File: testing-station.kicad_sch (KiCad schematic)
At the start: 0 parts

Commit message: added MAX31865 schematic page
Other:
- added sheet MAX31865 (MAX31865.kicad_sch)
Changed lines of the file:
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@@
 	(generator_version "8.0")
 	(paper "A4")
+	(sheet
+		(at 52.705 43.18)
+		(size 14.605 13.335)
+		(fields_autoplaced yes)
+		(stroke
+			(width 0.1524)
+			(type solid)
+		)
+		(fill
+			(color 0 0 0 0.0000)
+		)
+		(property "Sheetname" "MAX31865"
+			(at 52.705 42.4684 0)
+			(effects
+				(font
+					(size 1.27 1.27)
+				)
+				(justify left bottom)
+			)
+		)
+		(property "Sheetfile" "MAX31865.kicad_sch"
+			(at 52.705 57.0996 0)
+			(effects
+				(font
+					(size 1.27 1.27)
+				)
+				(justify left top)
+			)
+		)
+		(pin "SCK" input
+			(at 67.31 45.72 0)
+			(effects
+				(font
+					(size 1.27 1.27)
+				)
+				(justify right)
+			)
+		)
+		(pin "MISO" input
+			(at 67.31 48.26 0)
+			(effects
+				(font
+					(size 1.27 1.27)
+				)
+				(justify right)
+			)
+		)
+		(pin "CS" input
+			(at 67.31 50.8 0)
+			(effects
+				(font
+					(size 1.27 1.27)
+				)
+				(justify right)
+			)
+		)
+		(pin "MOSI" input
+			(at 67.31 53.34 0)
+			(effects
+				(font
+					(size 1.27 1.27)
+				)
+				(justify right)
+			)
+		)
+		(instances
+			(project "testing-station"
+				(path "/ed3950ec-e24f-4dd6-b9cc-eca012f1333b"
+					(page "2")
+				)
+			)
+		)
+	)
 	(sheet_instances
 		(path "/"

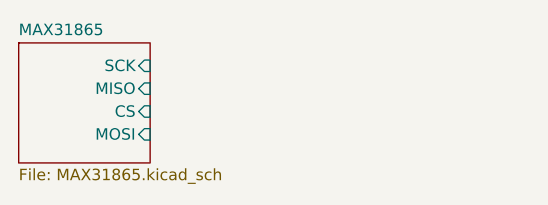
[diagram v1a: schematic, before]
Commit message: added BME680 schematic page
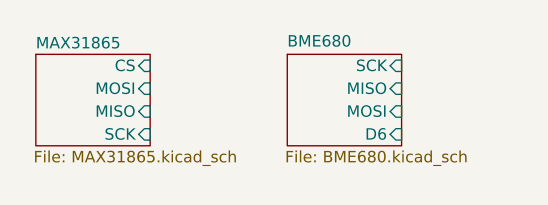
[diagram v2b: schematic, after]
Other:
- added sheet BME680 (BME680.kicad_sch)
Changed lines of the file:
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@@
 	(paper "A4")
 	(sheet
-		(at 52.705 43.18)
-		(size 14.605 13.335)
-		(fields_autoplaced yes)
+		(at 82.55 44.45)
+		(size 12.7 10.16)
+		(stroke
+			(width 0.1524)
+			(type solid)
+		)
+		(fill
+			(color 0 0 0 0.0000)
+		)
+		(property "Sheetname" "BME680"
+			(at 82.55 43.7384 0)
+			(effects
+				(font
+					(size 1.27 1.27)
+				)
+				(justify left bottom)
+			)
+		)
+		(property "Sheetfile" "BME680.kicad_sch"
+			(at 82.296 55.118 0)
+			(effects
+				(font
+					(size 1.27 1.27)
+				)
+				(justify left top)
+			)
+		)
+		(pin "MOSI" input
+			(at 95.25 50.8 0)
+			(effects
+				(font
+					(size 1.27 1.27)
+				)
+				(justify right)
+			)
+		)
+		(pin "D6" input
+			(at 95.25 53.34 0)
+			(effects
+				(font
+					(size 1.27 1.27)
+				)
+				(justify right)
+			)
+		)
+		(pin "MISO" input
+			(at 95.25 48.26 0)
+			(effects
+				(font
+					(size 1.27 1.27)
+				)
+				(justify right)
+			)
+		)
+		(pin "SCK" input
+			(at 95.25 45.72 0)
+			(effects
+				(font
+					(size 1.27 1.27)
+				)
+				(justify right)
+			)
+		)
+		(instances
+			(project "testing-station"
+				(path "/ed3950ec-e24f-4dd6-b9cc-eca012f1333b"
+					(page "3")
+				)
+			)
+		)
+	)
+	(sheet
+		(at 54.61 44.45)
+		(size 12.7 10.16)
 		(stroke
 			(width 0.1524)
@@
 		)
 		(property "Sheetname" "MAX31865"
-			(at 52.705 42.4684 0)
+			(at 54.61 43.942 0)
 			(effects
 				(font
@@
 		)
 		(property "Sheetfile" "MAX31865.kicad_sch"
-			(at 52.705 57.0996 0)
+			(at 54.356 55.118 0)
 			(effects
 				(font
@@
 		)
 		(pin "SCK" input
+			(at 67.31 53.34 0)
+			(effects
+				(font
+					(size 1.27 1.27)
+				)
+				(justify right)
+			)
+		)
+		(pin "MISO" input
+			(at 67.31 50.8 0)
+			(effects
+				(font
+					(size 1.27 1.27)
+				)
+				(justify right)
+			)
+		)
+		(pin "CS" input
 			(at 67.31 45.72 0)
 			(effects
@@
 			)
 		)
-		(pin "MISO" input
+		(pin "MOSI" input
 			(at 67.31 48.26 0)
 			(effects
 				(font
-					(size 1.27 1.27)
-				)
-				(justify right)
-			)
-		)
-		(pin "CS" input
-			(at 67.31 50.8 0)
-			(effects
-				(font
-					(size 1.27 1.27)
-				)
-				(justify right)
-			)
-		)
-		(pin "MOSI" input
-			(at 67.31 53.34 0)
-			(effects
-				(font

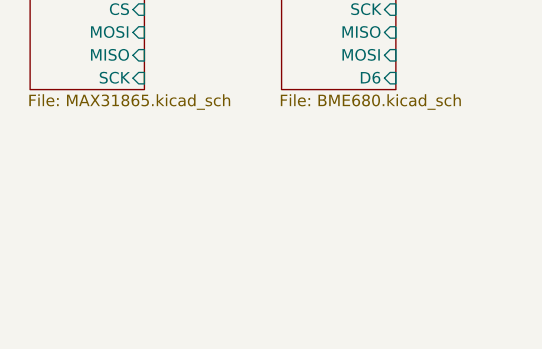
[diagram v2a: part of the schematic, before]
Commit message: added DS3231 schematic page
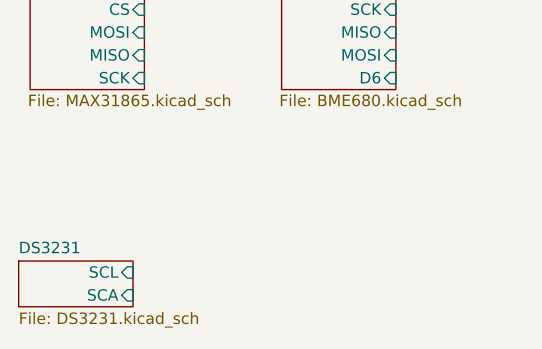
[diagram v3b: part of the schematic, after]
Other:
- added sheet DS3231 (DS3231.kicad_sch)
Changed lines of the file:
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@@
 	(paper "A4")
+	(sheet
+		(at 53.34 73.66)
+		(size 12.7 5.08)
+		(fields_autoplaced yes)
+		(stroke
+			(width 0.1524)
+			(type solid)
+		)
+		(fill
+			(color 0 0 0 0.0000)
+		)
+		(property "Sheetname" "DS3231"
+			(at 53.34 72.9484 0)
+			(effects
+				(font
+					(size 1.27 1.27)
+				)
+				(justify left bottom)
+			)
+		)
+		(property "Sheetfile" "DS3231.kicad_sch"
+			(at 53.34 79.3246 0)
+			(effects
+				(font
+					(size 1.27 1.27)
+				)
+				(justify left top)
+			)
+		)
+		(pin "SCL" input
+			(at 66.04 74.93 0)
+			(effects
+				(font
+					(size 1.27 1.27)
+				)
+				(justify right)
+			)
+		)
+		(pin "SCA" input
+			(at 66.04 77.47 0)
+			(effects
+				(font
+					(size 1.27 1.27)
+				)
+				(justify right)
+			)
+		)
+		(instances
+			(project "testing-station"
+				(path "/ed3950ec-e24f-4dd6-b9cc-eca012f1333b"
+					(page "4")
+				)
+			)
+		)
+	)
 	(sheet
 		(at 82.55 44.45)

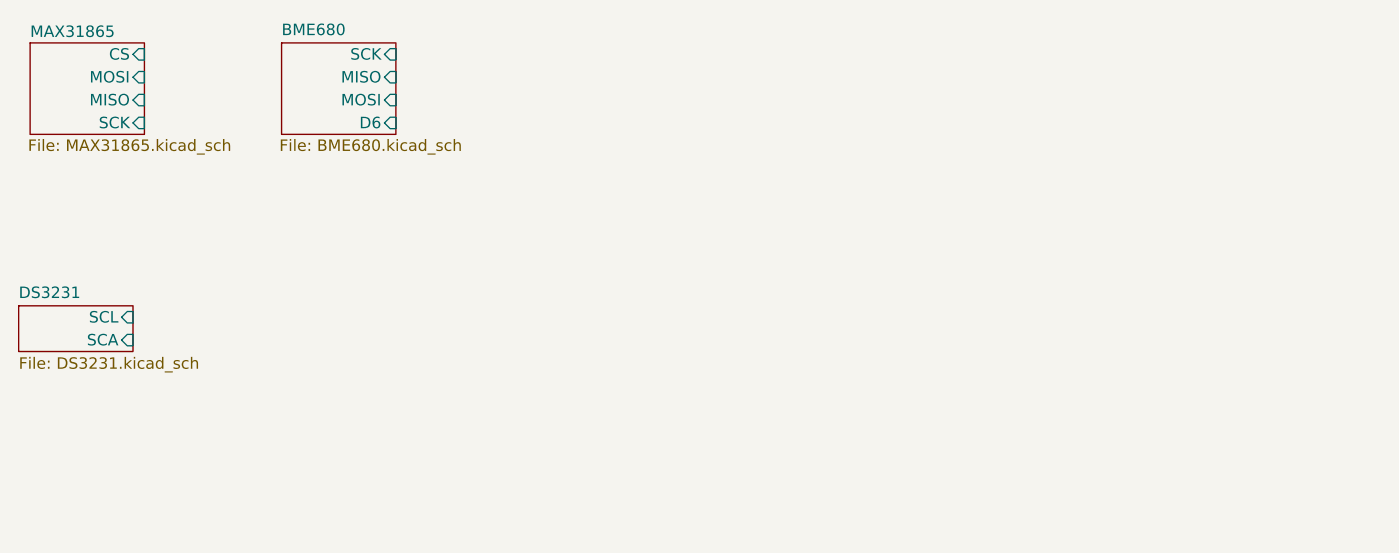
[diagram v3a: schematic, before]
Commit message: added 2 more MAX31865
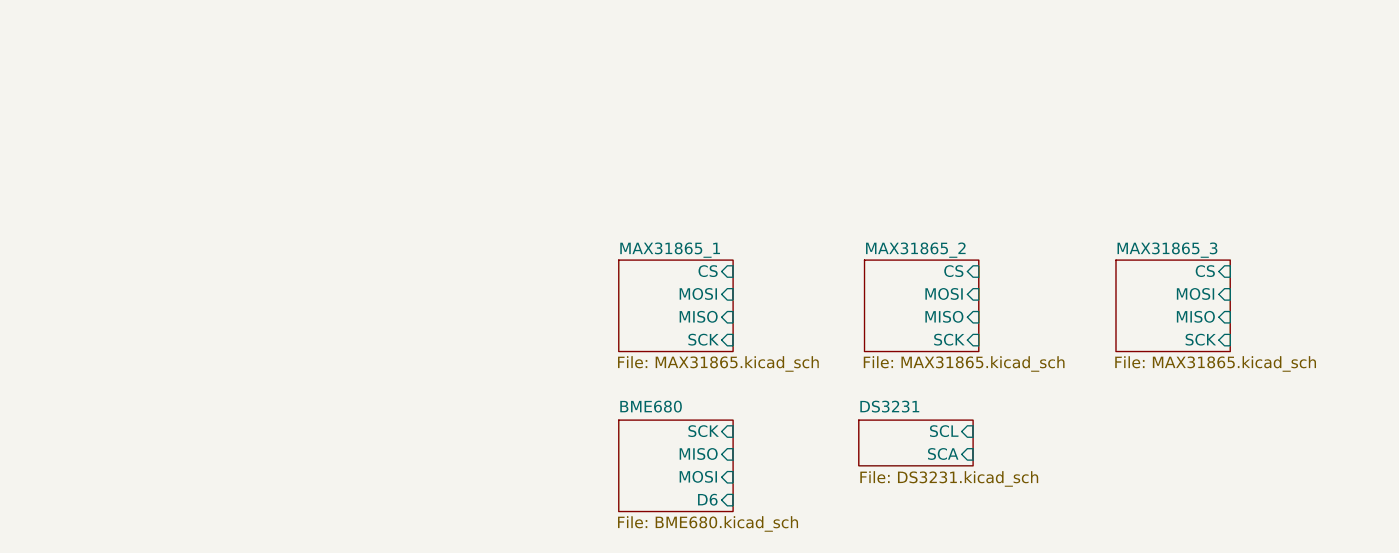
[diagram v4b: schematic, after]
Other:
- sheet MAX31865 renamed MAX31865_1
- added sheet MAX31865_2 (MAX31865.kicad_sch)
- added sheet MAX31865_3 (MAX31865.kicad_sch)
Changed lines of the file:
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@@
 	(paper "A4")
 	(sheet
-		(at 53.34 73.66)
+		(at 175.26 68.58)
+		(size 12.7 10.16)
+		(stroke
+			(width 0.1524)
+			(type solid)
+		)
+		(fill
+			(color 0 0 0 0.0000)
+		)
+		(property "Sheetname" "MAX31865_3"
+			(at 175.26 68.072 0)
+			(effects
+				(font
+					(size 1.27 1.27)
+				)
+				(justify left bottom)
+			)
+		)
+		(property "Sheetfile" "MAX31865.kicad_sch"
+			(at 175.006 79.248 0)
+			(effects
+				(font
+					(size 1.27 1.27)
+				)
+				(justify left top)
+			)
+		)
+		(pin "SCK" input
+			(at 187.96 77.47 0)
+			(effects
+				(font
+					(size 1.27 1.27)
+				)
+				(justify right)
+			)
+		)
+		(pin "MISO" input
+			(at 187.96 74.93 0)
+			(effects
+				(font
+					(size 1.27 1.27)
+				)
+				(justify right)
+			)
+		)
+		(pin "CS" input
+			(at 187.96 69.85 0)
+			(effects
+				(font
+					(size 1.27 1.27)
+				)
+				(justify right)
+			)
+		)
+		(pin "MOSI" input
+			(at 187.96 72.39 0)
+			(effects
+				(font
+					(size 1.27 1.27)
+				)
+				(justify right)
+			)
+		)
+		(instances
+			(project "testing-station"
+				(path "/ed3950ec-e24f-4dd6-b9cc-eca012f1333b"
+					(page "4")
+				)
+			)
+		)
+	)
+	(sheet
+		(at 146.685 86.36)
 		(size 12.7 5.08)
 		(fields_autoplaced yes)
@@
 		)
 		(property "Sheetname" "DS3231"
-			(at 53.34 72.9484 0)
+			(at 146.685 85.6484 0)
 			(effects
 				(font
@@
 		)
 		(property "Sheetfile" "DS3231.kicad_sch"
-			(at 53.34 79.3246 0)
+			(at 146.685 92.0246 0)
 			(effects
 				(font
@@
 		)
 		(pin "SCL" input
-			(at 66.04 74.93 0)
+			(at 159.385 87.63 0)
 			(effects
 				(font
@@
 		)
 		(pin "SCA" input
-			(at 66.04 77.47 0)
-			(effects
-				(font
-					(size 1.27 1.27)
-				)
-				(justify right)
-			)
-		)
-		(instances
-			(project "testing-station"
-				(path "/ed3950ec-e24f-4dd6-b9cc-eca012f1333b"
-					(page "4")
+			(at 159.385 90.17 0)
+			(effects
+				(font
+					(size 1.27 1.27)
+				)
+				(justify right)
+			)
+		)
+		(instances
+			(project "testing-station"
+				(path "/ed3950ec-e24f-4dd6-b9cc-eca012f1333b"
+					(page "6")
 				)
 			)
@@
 	)
 	(sheet
-		(at 82.55 44.45)
+		(at 120.015 86.36)
 		(size 12.7 10.16)
 		(stroke
@@
 		)
 		(property "Sheetname" "BME680"
-			(at 82.55 43.7384 0)
+			(at 120.015 85.6484 0)
 			(effects
 				(font
@@
 		)
 		(property "Sheetfile" "BME680.kicad_sch"
-			(at 82.296 55.118 0)
+			(at 119.761 97.028 0)
 			(effects
 				(font
@@
 		)
 		(pin "MOSI" input
-			(at 95.25 50.8 0)
+			(at 132.715 92.71 0)
 			(effects
 				(font
@@
 		)
 		(pin "D6" input
-			(at 95.25 53.34 0)
+			(at 132.715 95.25 0)
 			(effects
 				(font
@@
 		)
 		(pin "MISO" input
-			(at 95.25 48.26 0)
+			(at 132.715 90.17 0)
 			(effects
 				(font
@@
 		)
 		(pin "SCK" input
-			(at 95.25 45.72 0)
+			(at 132.715 87.63 0)
+			(effects
+				(font
+					(size 1.27 1.27)
+				)
+				(justify right)
+			)
+		)
+		(instances
+			(project "testing-station"
+				(path "/ed3950ec-e24f-4dd6-b9cc-eca012f1333b"
+					(page "5")
+				)
+			)
+		)
+	)
+	(sheet
+		(at 120.015 68.58)
+		(size 12.7 10.16)
+		(stroke
+			(width 0.1524)
+			(type solid)
+		)
+		(fill
+			(color 0 0 0 0.0000)
+		)
+		(property "Sheetname" "MAX31865_1"
+			(at 120.015 68.072 0)
+			(effects
+				(font
+					(size 1.27 1.27)
+				)
+				(justify left bottom)
+			)
+		)
+		(property "Sheetfile" "MAX31865.kicad_sch"
+			(at 119.761 79.248 0)
+			(effects
+				(font
+					(size 1.27 1.27)
+				)
+				(justify left top)
+			)
+		)
+		(pin "SCK" input
+			(at 132.715 77.47 0)
+			(effects
+				(font
+					(size 1.27 1.27)
+				)
+				(justify right)
+			)
+		)
+		(pin "MISO" input
+			(at 132.715 74.93 0)
+			(effects
+				(font
+					(size 1.27 1.27)
+				)
+				(justify right)
+			)
+		)
+		(pin "CS" input
+			(at 132.715 69.85 0)
+			(effects
+				(font
+					(size 1.27 1.27)
+				)
+				(justify right)
+			)
+		)
+		(pin "MOSI" input
+			(at 132.715 72.39 0)
+			(effects
+				(font
+					(size 1.27 1.27)
+				)
+				(justify right)
+			)
+		)
+		(instances
+			(project "testing-station"
+				(path "/ed3950ec-e24f-4dd6-b9cc-eca012f1333b"
+					(page "2")
+				)
+			)
+		)
+	)
+	(sheet
+		(at 147.32 68.58)
+		(size 12.7 10.16)
+		(stroke
+			(width 0.1524)
+			(type solid)
+		)
+		(fill
+			(color 0 0 0 0.0000)
+		)
+		(property "Sheetname" "MAX31865_2"
+			(at 147.32 68.072 0)
+			(effects
+				(font
+					(size 1.27 1.27)
+				)
+				(justify left bottom)
+			)
+		)
+		(property "Sheetfile" "MAX31865.kicad_sch"
+			(at 147.066 79.248 0)
+			(effects
+				(font
+					(size 1.27 1.27)
+				)
+				(justify left top)
+			)
+		)
+		(pin "SCK" input
+			(at 160.02 77.47 0)
+			(effects
+				(font
+					(size 1.27 1.27)
+				)
+				(justify right)
+			)
+		)
+		(pin "MISO" input
+			(at 160.02 74.93 0)
+			(effects
+				(font
+					(size 1.27 1.27)
+				)
+				(justify right)
+			)
+		)
+		(pin "CS" input
+			(at 160.02 69.85 0)
+			(effects
+				(font
+					(size 1.27 1.27)
+				)
+				(justify right)
+			)
+		)
+		(pin "MOSI" input
+			(at 160.02 72.39 0)
 			(effects
 				(font
@@
 				)
 			)
-		)
-	)
-	(sheet
-		(at 54.61 44.45)
-		(size 12.7 10.16)
-		(stroke
-			(width 0.1524)
-			(type solid)
-		)
-		(fill
-			(color 0 0 0 0.0000)
-		)
-		(property "Sheetname" "MAX31865"
-			(at 54.61 43.942 0)
-			(effects
-				(font
-					(size 1.27 1.27)
-				)
-				(justify left bottom)
-			)
-		)
-		(property "Sheetfile" "MAX31865.kicad_sch"
-			(at 54.356 55.118 0)
-			(effects
-				(font
-					(size 1.27 1.27)
-				)
-				(justify left top)
-			)
-		)
-		(pin "SCK" input
-			(at 67.31 53.34 0)
-			(effects
-				(font
-					(size 1.27 1.27)
-				)
-				(justify right)
-			)
-		)
-		(pin "MISO" input
-			(at 67.31 50.8 0)
-			(effects
-				(font
-					(size 1.27 1.27)
-				)
-				(justify right)
-			)
-		)
-		(pin "CS" input
-			(at 67.31 45.72 0)
-			(effects
-				(font
-					(size 1.27 1.27)
-				)
-				(justify right)
-			)
-		)
-		(pin "MOSI" input
-			(at 67.31 48.26 0)
-			(effects
-				(font
-					(size 1.27 1.27)
-				)
-				(justify right)
-			)
-		)
-		(instances
-			(project "testing-station"
-				(path "/ed3950ec-e24f-4dd6-b9cc-eca012f1333b"
-					(page "2")
-				)
-			)
